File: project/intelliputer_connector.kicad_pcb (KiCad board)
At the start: 2 copper layers, 68.1 x 98.9 mm, 2 parts, among them J1 44-contact card edge, J2 Ribbon header, 2x22, 2.54 mm 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

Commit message: Add checked Intelliputer Connector Gerbers
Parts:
- J1: footprint Ribbon_Card:CardEdge_2x22_2.54mm -> CardEdge_2x22_2.54mm
- J2: footprint Connector_PinHeader_2.54mm:PinHeader_2x22_P2.54mm_Vertical -> PinHeader_22x2_2.54mm_Vertical
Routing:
- net CARD_35: track 80.5 -> 82.4 mm
- net CARD_21: track 80.5 -> 82.4 mm
- net CARD_17: track 80.5 -> 82.4 mm
- net CARD_11: track 80.5 -> 82.4 mm
- net CARD_09: track 80.5 -> 82.4 mm
- net CARD_05: track 80.5 -> 82.4 mm
- net CARD_03: track 80.5 -> 82.4 mm
- net CARD_01: track 80.5 -> 82.4 mm
- net CARD_43: track 80.5 -> 82.4 mm
- net CARD_41: track 80.5 -> 82.4 mm
- net CARD_39: track 80.5 -> 82.4 mm
- net CARD_37: track 80.5 -> 82.4 mm
- net CARD_33: track 80.5 -> 82.4 mm
- net CARD_31: track 80.5 -> 82.4 mm
- net CARD_29: track 80.5 -> 82.4 mm
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
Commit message: Change silkscreen
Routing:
- net CARD_14: track 78.0 -> 0.00 mm
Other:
- board text added: "cartheur"
- board text removed: "DIRECT 1:1 · J1 n → J2 n · 1.6 mm PCB · Intellivision cartridge profile"

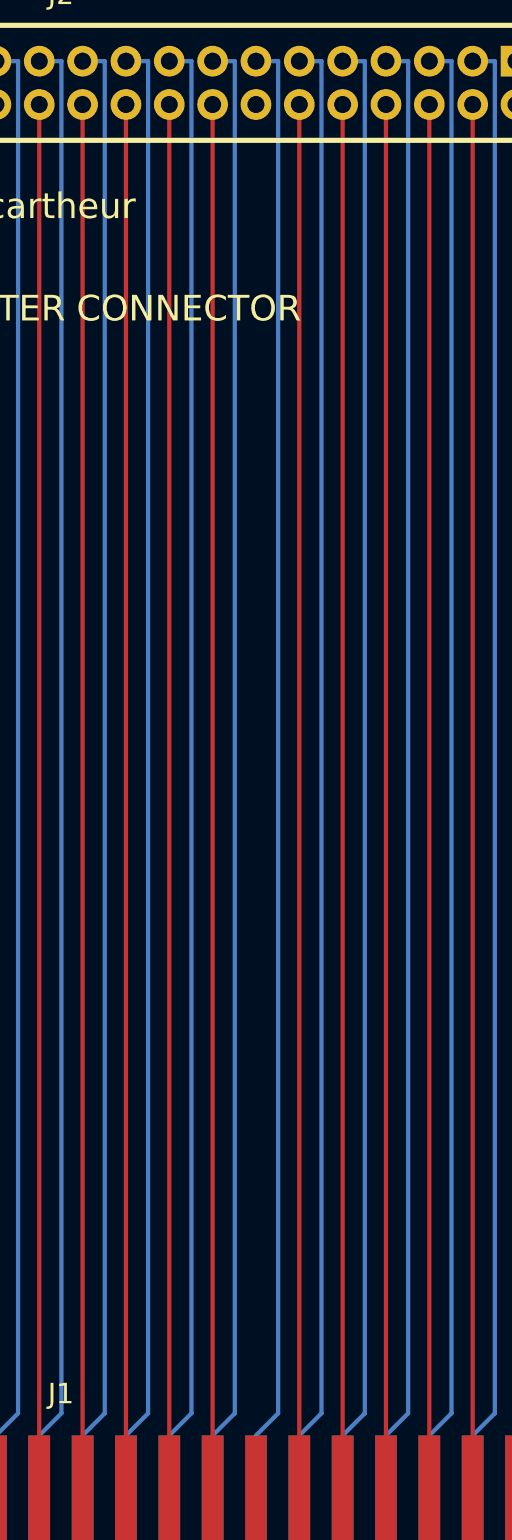
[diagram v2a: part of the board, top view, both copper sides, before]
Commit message: fix: restore CARD_14 trace and regenerate fabrication package
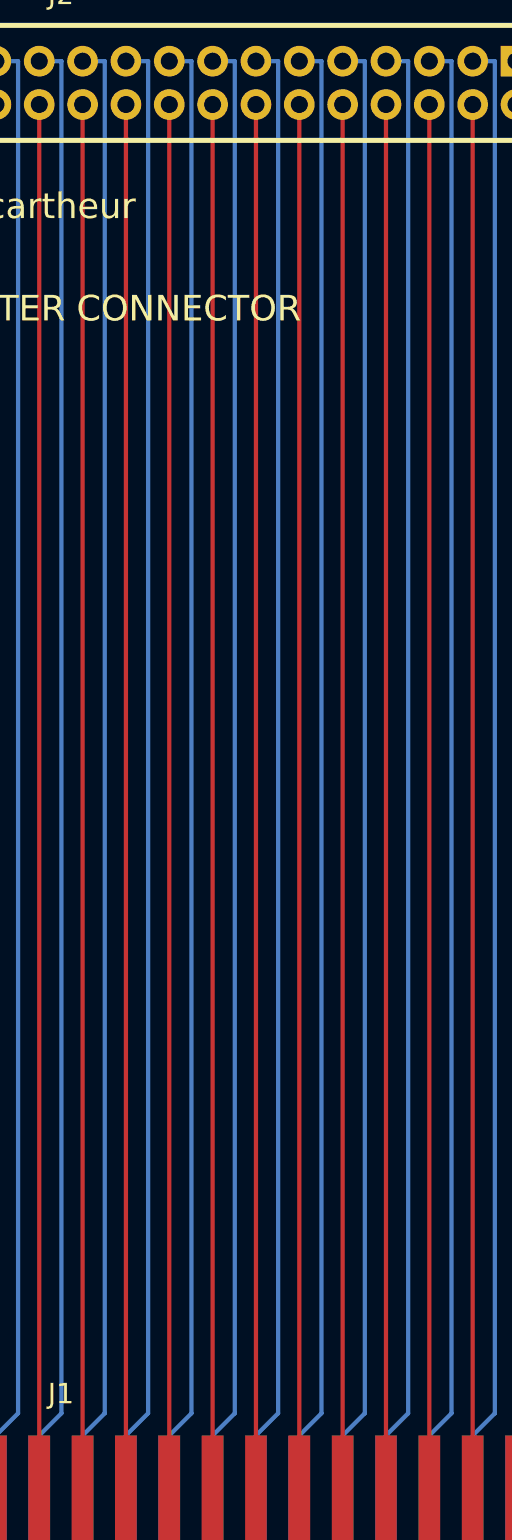
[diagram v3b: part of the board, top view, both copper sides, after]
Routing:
- net CARD_14: track 0.00 -> 78.0 mm
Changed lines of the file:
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@@
+	)
+	(segment
+		(start 129.4257 183.54)
+		(end 129.4257 105.54)
+		(width 0.25)
+		(layer "F.Cu")
+		(net "CARD_14")
 	)
 	(segment

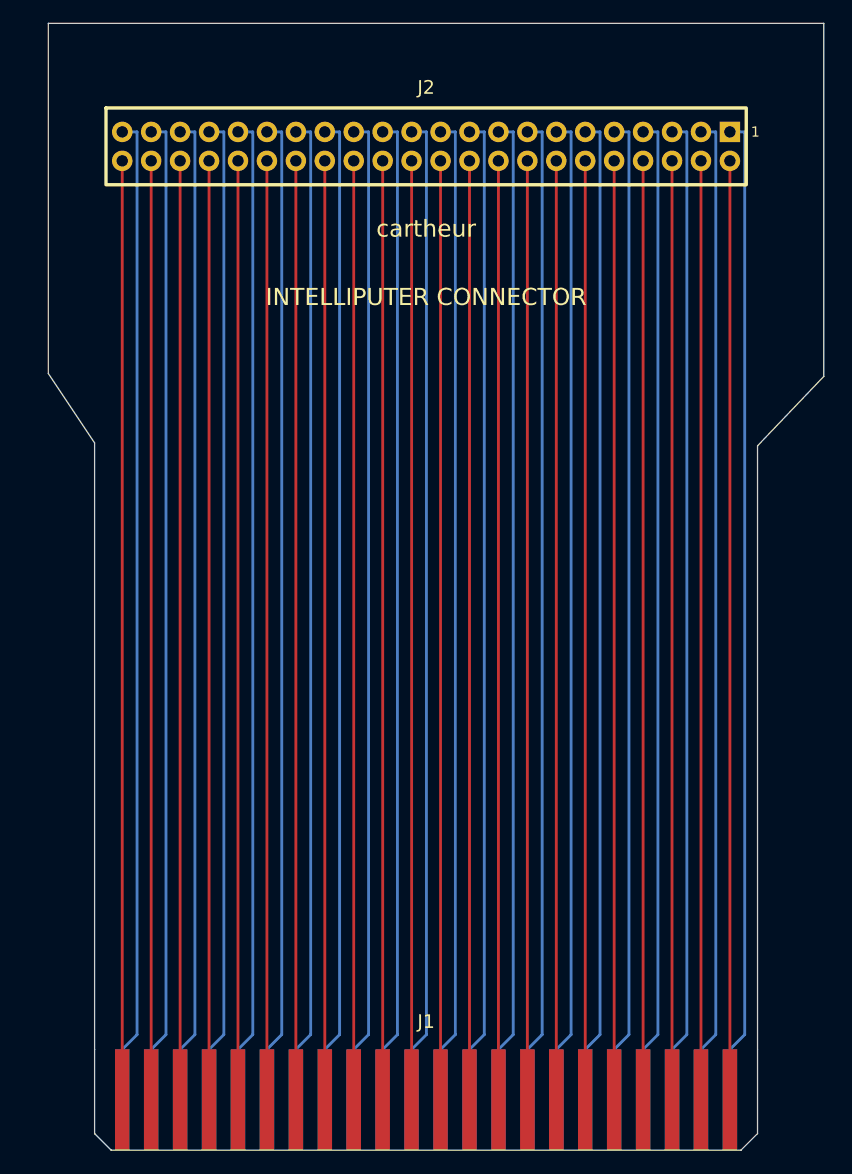
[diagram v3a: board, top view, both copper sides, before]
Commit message: feat: shorten connector board and add silkscreen artwork
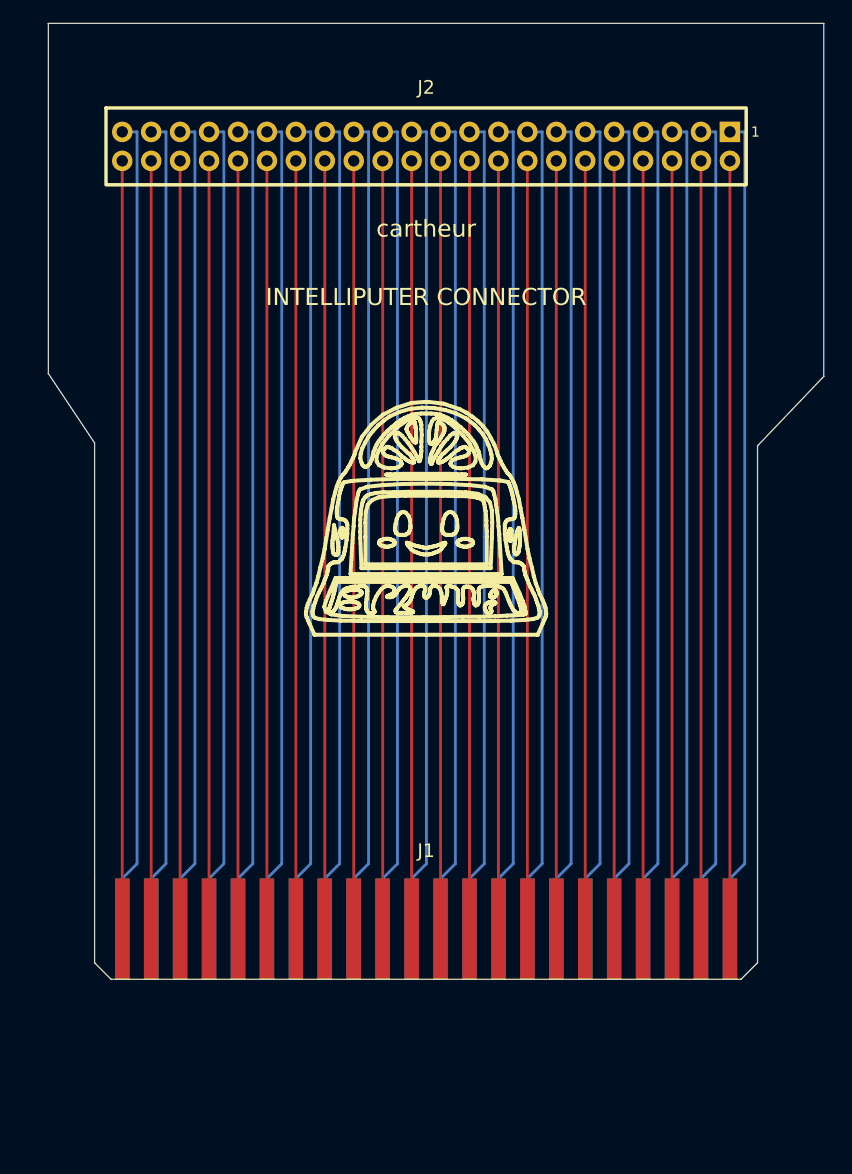
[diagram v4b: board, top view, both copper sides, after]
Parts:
- moved J1 15.0 mm to (0.00, -15.0)
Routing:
- net CARD_44: track 78.0 -> 63.0 mm
- net CARD_43: track 82.4 -> 67.4 mm
- net CARD_42: track 78.0 -> 63.0 mm
- net CARD_41: track 82.4 -> 67.4 mm
- net CARD_40: track 78.0 -> 63.0 mm
- net CARD_39: track 82.4 -> 67.4 mm
- net CARD_38: track 78.0 -> 63.0 mm
- net CARD_37: track 82.4 -> 67.4 mm
- net CARD_36: track 78.0 -> 63.0 mm
- net CARD_35: track 82.4 -> 67.4 mm
- net CARD_34: track 78.0 -> 63.0 mm
- net CARD_33: track 82.4 -> 67.4 mm
- net CARD_32: track 78.0 -> 63.0 mm
- net CARD_31: track 82.4 -> 67.4 mm
- net CARD_30: track 78.0 -> 63.0 mm
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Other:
- board size 68.1 x 98.9 mm -> 68.1 x 83.9 mm

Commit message: Finalize Intellivision connector pinout and fabrication package
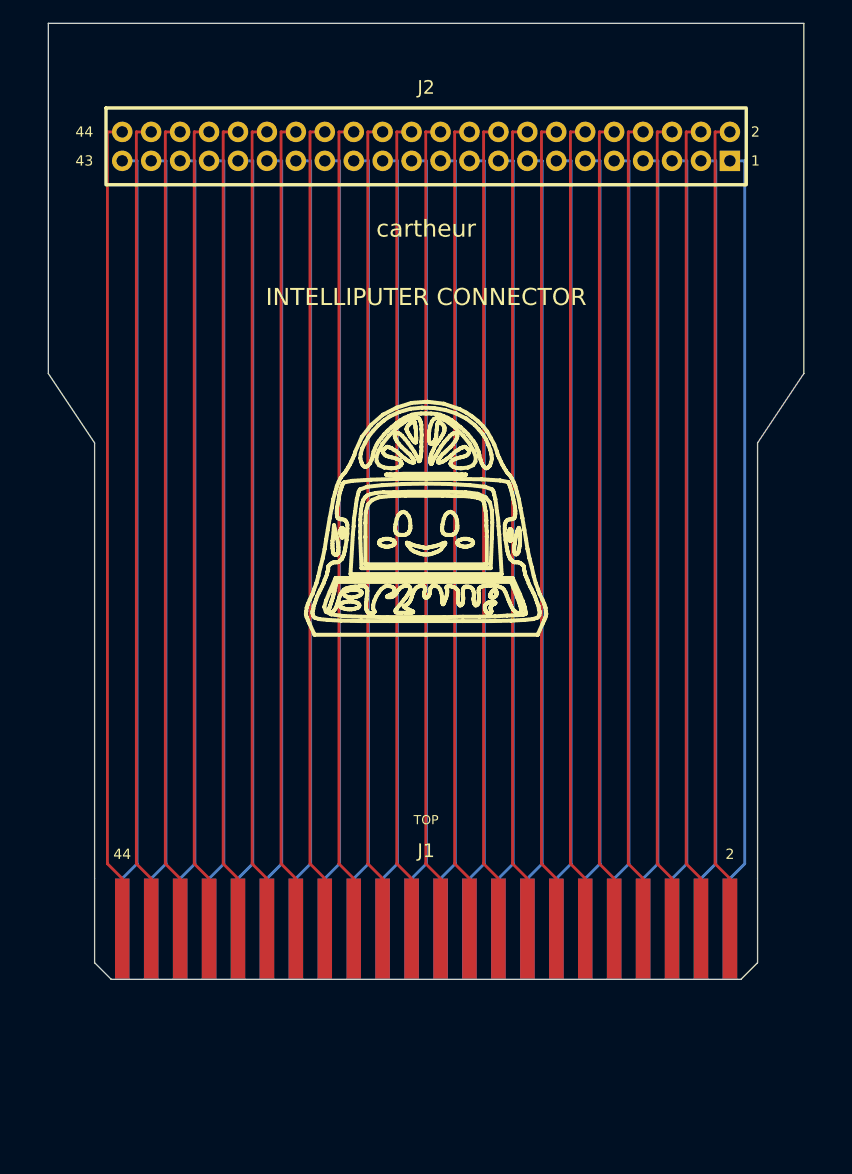
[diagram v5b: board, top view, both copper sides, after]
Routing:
- net CARD_32: track 63.0 -> 67.4 mm
- net CARD_28: track 63.0 -> 67.4 mm
- net CARD_14: track 63.0 -> 67.4 mm
- net CARD_12: track 63.0 -> 67.4 mm
- net CARD_08: track 63.0 -> 67.4 mm
- net CARD_06: track 63.0 -> 67.4 mm
- net CARD_44: track 63.0 -> 67.4 mm
- net CARD_42: track 63.0 -> 67.4 mm
- net CARD_40: track 63.0 -> 67.4 mm
- net CARD_38: track 63.0 -> 67.4 mm
- net CARD_36: track 63.0 -> 67.4 mm
- net CARD_34: track 63.0 -> 67.4 mm
- net CARD_30: track 63.0 -> 67.4 mm
- net CARD_26: track 63.0 -> 67.4 mm
- net CARD_24: track 63.0 -> 67.4 mm
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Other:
- board size 68.1 x 83.9 mm -> 66.3 x 83.9 mm
- board text added: "01 GND / 02 GND/VID"
- board text added: "03 ~MSYNC / 04 CBLNK"
- board text added: "05 DB7 / 06 EXT AUD"
- board text added: "07 DB8 / 08 EXT VID"
- board text added: "09 DB6 / 10 MCLK"
- board text added: "1"
- board text added: "11 DB9 / 12 RESET"
- board text added: "13 DB5 / 14 SR1"
- board text added: "15 DB10 / 16 SER OUT"
- board text added: "17 DB4 / 18 SER IN"
- board text added: "19 DB11 / 20 ROM DIS"
- board text added: "2"
- board text added: "21 DB3 / 22 GND"
- board text added: "23 DB12 / 24 GND"
- board text added: "25 DB13 / 26 GND"
- board text added: "27 DB2 / 28 GND"
- board text added: "29 DB14 / 30 ~BUSAK"
- board text added: "31 DB1 / 32 BC1 IN"
- board text added: "33 DB0 / 34 BC2 IN"
- board text added: "35 DB15 / 36 BDIR IN"
- board text added: "37 BDIR OUT / 38 BDIR OUT"
- board text added: "39 BC2 OUT / 40 BC2 OUT"
- board text added: "41 BC1 OUT / 42 BC1 OUT"
- board text added: "43"
- board text added: "43 +5V / 44 GND"
- board text added: "44"
- board text added: "TOP"

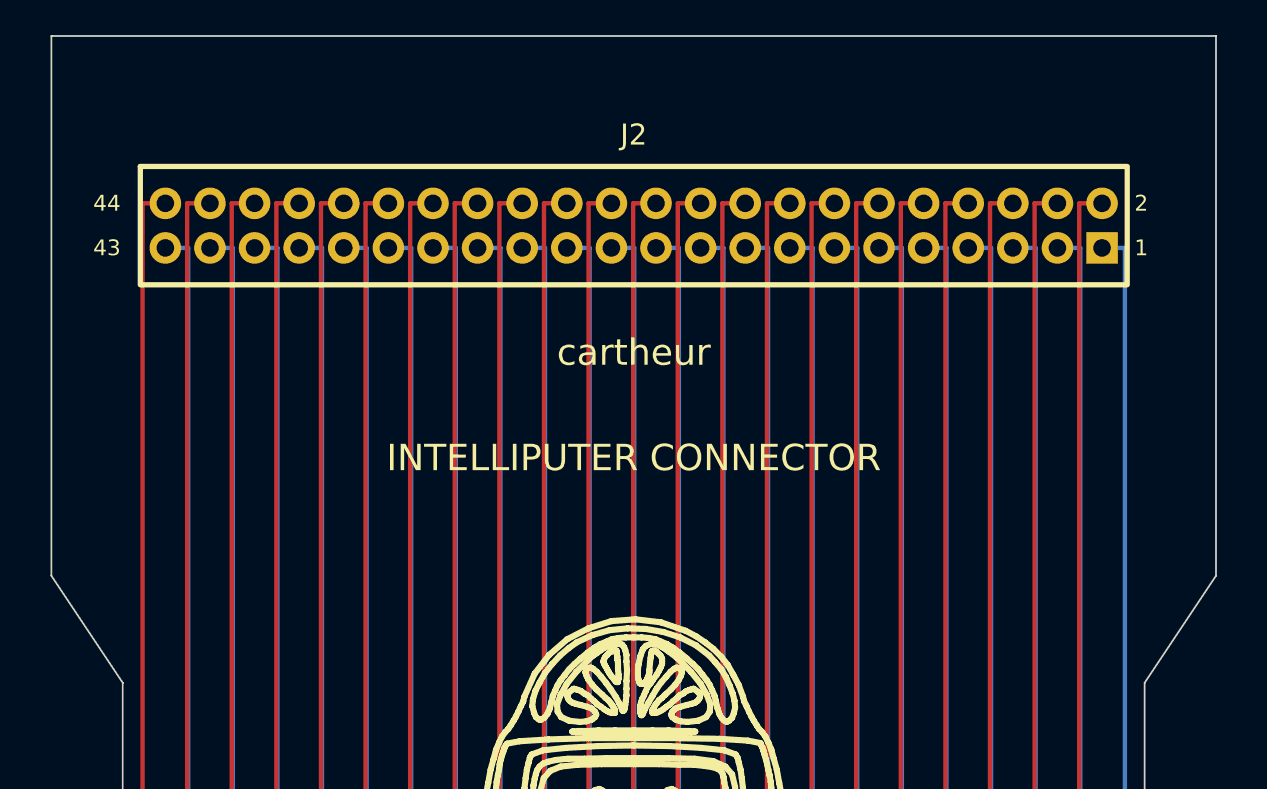
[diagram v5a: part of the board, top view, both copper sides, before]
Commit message: Restore required symmetric board outline
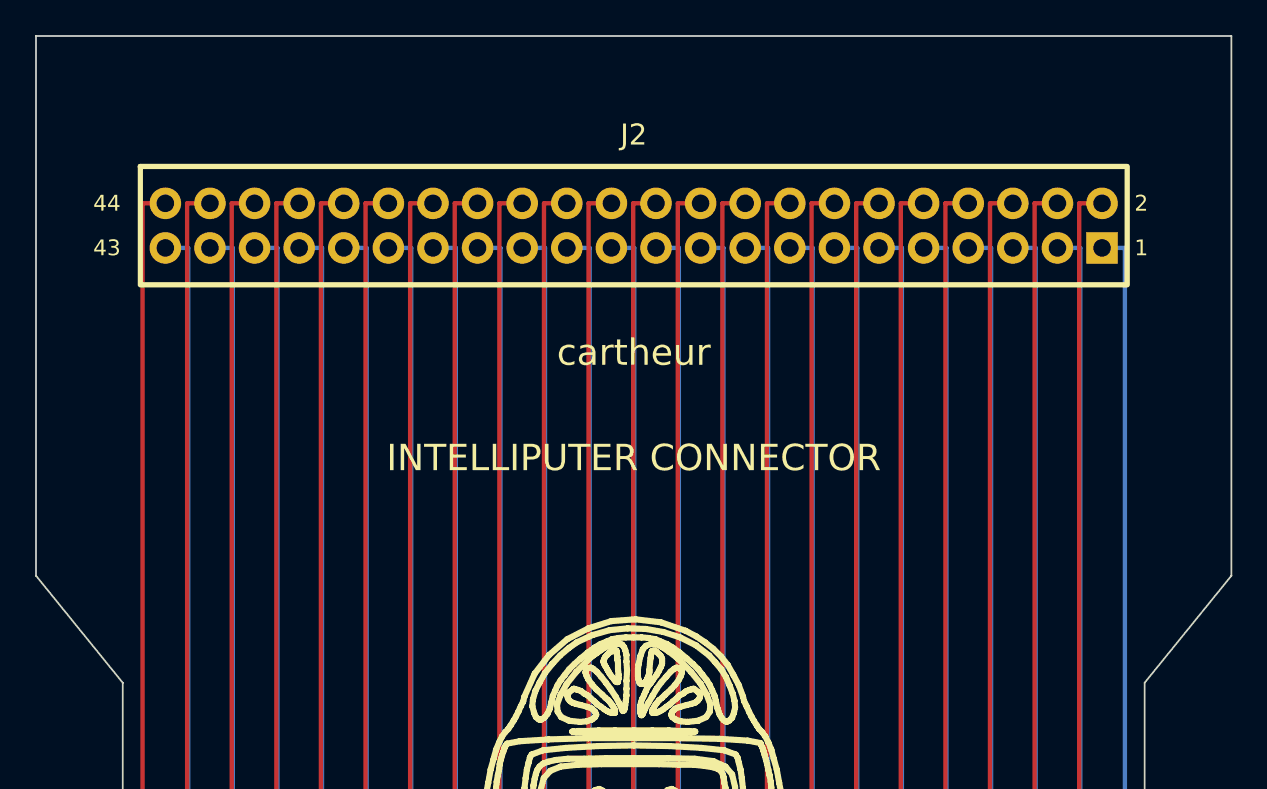
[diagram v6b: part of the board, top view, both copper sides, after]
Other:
- board size 66.3 x 83.9 mm -> 68.1 x 83.9 mm
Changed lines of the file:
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@@
 	)
 	(gr_line
-		(start 84.836 93.472)
-		(end 151.1554 93.472)
+		(start 83.9597 93.472)
+		(end 152.0317 93.472)
 		(stroke
 			(width 0.1)
@@
 	)
 	(gr_line
-		(start 84.836 124.206)
-		(end 84.836 93.472)
+		(start 83.9597 124.206)
+		(end 83.9597 93.472)
 		(stroke
 			(width 0.1)
@@
 	(gr_line
 		(start 88.9 130.302)
-		(end 84.836 124.206)
+		(end 83.9597 124.206)
 		(stroke
 			(width 0.1)
@@
 	)
 	(gr_line
-		(start 151.1554 93.472)
-		(end 151.1554 124.206)
+		(start 152.0317 93.472)
+		(end 152.0317 124.206)
 		(stroke
 			(width 0.1)
@@
 	)
 	(gr_line
-		(start 151.1554 124.206)
+		(start 152.0317 124.206)
 		(end 147.0914 130.302)
 		(stroke
